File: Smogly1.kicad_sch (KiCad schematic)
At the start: 9 parts, among them J1 VCC IN, J10 NodeMCU A0-VIN, J11 NodeMCU D0-3.3V, J2 PMSx003, J3 BME280, J4 microUSB, J5 5/3.3/GND, J6 DeepSleep, J8 D5/6/7/8

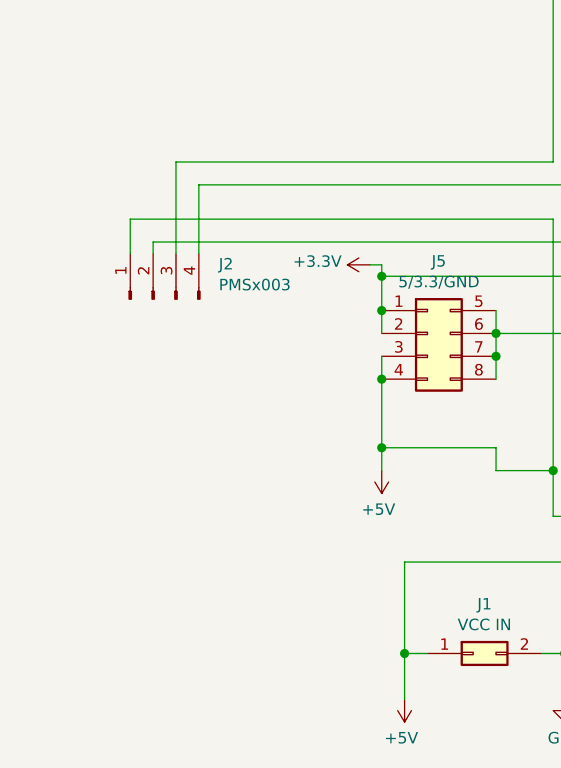
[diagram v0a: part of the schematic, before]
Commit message: added PMS7003 connector
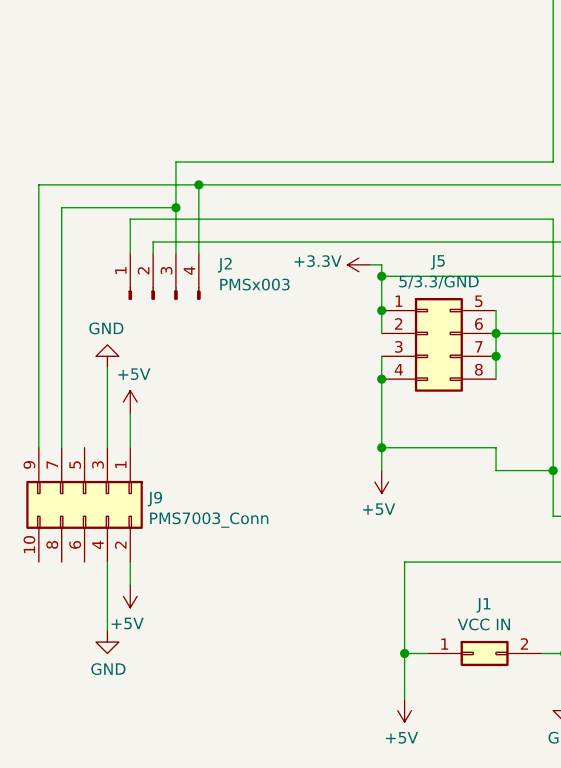
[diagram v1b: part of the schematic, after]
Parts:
- added J9: PMS7003_Conn, Connector_PinSocket_1.27mm:PinSocket_2x05_P1.27mm_Vertical, symbol Connector_Generic:Conn_02x05_Odd_Even
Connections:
- net +5V: now also J9.1 (Pin_1), J9.2 (Pin_2)
- net GND: now also J9.3 (Pin_3), J9.4 (Pin_4)
- net at J11.3 (Pin_3), J2.3 (Pin_3): now also J9.7 (Pin_7)
- net at J11.2 (Pin_2), J2.4 (Pin_4): now also J9.9 (Pin_9)
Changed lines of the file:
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@@
-(kicad_sch (version 20210126) (generator eeschema)
+(kicad_sch (version 20210406) (generator eeschema)
   (paper "A4")
+  (junction (at 88.9 123.19) (diameter 1.016) (color 0 0 0 0))
+  (junction (at 91.44 120.65) (diameter 1.016) (color 0 0 0 0))
   (junction (at 111.76 130.81) (diameter 1.016) (color 0 0 0 0))
   (junction (at 111.76 134.62) (diameter 1.016) (color 0 0 0 0))
@@
   (junction (at 132.08 172.72) (diameter 1.016) (color 0 0 0 0))
   (junction (at 133.35 137.16) (diameter 1.016) (color 0 0 0 0))
+  (wire (pts (xy 73.66 120.65) (xy 73.66 149.86))
+    (stroke (width 0) (type solid) (color 0 0 0 0))
+  )
+  (wire (pts (xy 76.2 123.19) (xy 76.2 149.86))
+    (stroke (width 0) (type solid) (color 0 0 0 0))
+  )
+  (wire (pts (xy 81.28 140.97) (xy 81.28 149.86))
+    (stroke (width 0) (type solid) (color 0 0 0 0))
+  )
+  (wire (pts (xy 81.28 162.56) (xy 81.28 170.18))
+    (stroke (width 0) (type solid) (color 0 0 0 0))
+  )
   (wire (pts (xy 83.82 124.46) (xy 83.82 128.27))
     (stroke (width 0) (type solid) (color 0 0 0 0))
   )
+  (wire (pts (xy 83.82 146.05) (xy 83.82 149.86))
+    (stroke (width 0) (type solid) (color 0 0 0 0))
+  )
+  (wire (pts (xy 83.82 162.56) (xy 83.82 165.1))
+    (stroke (width 0) (type solid) (color 0 0 0 0))
+  )
   (wire (pts (xy 86.36 127) (xy 86.36 128.27))
     (stroke (width 0) (type solid) (color 0 0 0 0))
   )
-  (wire (pts (xy 88.9 118.11) (xy 88.9 128.27))
+  (wire (pts (xy 88.9 118.11) (xy 88.9 123.19))
+    (stroke (width 0) (type solid) (color 0 0 0 0))
+  )
+  (wire (pts (xy 88.9 123.19) (xy 76.2 123.19))
+    (stroke (width 0) (type solid) (color 0 0 0 0))
+  )
+  (wire (pts (xy 88.9 123.19) (xy 88.9 128.27))
+    (stroke (width 0) (type solid) (color 0 0 0 0))
+  )
+  (wire (pts (xy 91.44 120.65) (xy 73.66 120.65))
     (stroke (width 0) (type solid) (color 0 0 0 0))
   )
@@
   (wire (pts (xy 250.19 113.03) (xy 254 113.03))
     (stroke (width 0) (type solid) (color 0 0 0 0))
+  )
+  (symbol (lib_id "power:+5V") (at 83.82 146.05 0) (unit 1)
+    (in_bom yes) (on_board yes)
+    (property "Reference" "#PWR0109" (id 0) (at 83.82 149.86 0)
+      (effects (font (size 1.27 1.27)) hide)
+    )
+    (property "Value" "+5V" (id 1) (at 84.1883 141.7256 0))
+    (property "Footprint" "" (id 2) (at 83.82 146.05 0)
+      (effects (font (size 1.27 1.27)) hide)
+    )
+    (property "Datasheet" "" (id 3) (at 83.82 146.05 0)
+      (effects (font (size 1.27 1.27)) hide)
+    )
+    (pin "1")
+  )
+  (symbol (lib_id "power:+5V") (at 83.82 165.1 180) (unit 1)
+    (in_bom yes) (on_board yes)
+    (property "Reference" "#PWR0106" (id 0) (at 83.82 161.29 0)
+      (effects (font (size 1.27 1.27)) hide)
+    )
+    (property "Value" "+5V" (id 1) (at 83.4517 169.4244 0))
+    (property "Footprint" "" (id 2) (at 83.82 165.1 0)
+      (effects (font (size 1.27 1.27)) hide)
+    )
+    (property "Datasheet" "" (id 3) (at 83.82 165.1 0)
+      (effects (font (size 1.27 1.27)) hide)
+    )
+    (pin "1")
   )
   (symbol (lib_id "power:+3.3V") (at 110.49 129.54 90) (unit 1)
@@
     )
     (property "Datasheet" "" (id 3) (at 114.3 177.8 0)
+      (effects (font (size 1.27 1.27)) hide)
+    )
+    (pin "1")
+  )
+  (symbol (lib_id "power:GND") (at 81.28 140.97 180) (unit 1)
+    (in_bom yes) (on_board yes)
+    (property "Reference" "#PWR0108" (id 0) (at 81.28 134.62 0)
+      (effects (font (size 1.27 1.27)) hide)
+    )
+    (property "Value" "GND" (id 1) (at 81.1657 136.6456 0))
+    (property "Footprint" "" (id 2) (at 81.28 140.97 0)
+      (effects (font (size 1.27 1.27)) hide)
+    )
+    (property "Datasheet" "" (id 3) (at 81.28 140.97 0)
+      (effects (font (size 1.27 1.27)) hide)
+    )
+    (pin "1")
+  )
+  (symbol (lib_id "power:GND") (at 81.28 170.18 0) (unit 1)
+    (in_bom yes) (on_board yes)
+    (property "Reference" "#PWR0107" (id 0) (at 81.28 176.53 0)
+      (effects (font (size 1.27 1.27)) hide)
+    )
+    (property "Value" "GND" (id 1) (at 81.3943 174.5044 0))
+    (property "Footprint" "" (id 2) (at 81.28 170.18 0)
+      (effects (font (size 1.27 1.27)) hide)
+    )
+    (property "Datasheet" "" (id 3) (at 81.28 170.18 0)
       (effects (font (size 1.27 1.27)) hide)
     )
@@
     (pin "7")
     (pin "8")
+  )
+  (symbol (lib_id "Connector_Generic:Conn_02x05_Odd_Even") (at 78.74 154.94 270) (unit 1)
+    (in_bom yes) (on_board yes) (fields_autoplaced)
+    (property "Reference" "J9" (id 0) (at 85.8521 155.4491 90)
+      (effects (font (size 1.27 1.27)) (justify left))
+    )
+    (property "Value" "PMS7003_Conn" (id 1) (at 85.8521 157.7478 90)
+      (effects (font (size 1.27 1.27)) (justify left))
+    )
+    (property "Footprint" "Connector_PinSocket_1.27mm:PinSocket_2x05_P1.27mm_Vertical" (id 2) (at 78.74 154.94 0)
+      (effects (font (size 1.27 1.27)) hide)
+    )
+    (property "Datasheet" "~" (id 3) (at 78.74 154.94 0)
+      (effects (font (size 1.27 1.27)) hide)
+    )
+    (pin "1")
+    (pin "10")
+    (pin "2")
+    (pin "3")
+    (pin "4")
+    (pin "5")
+    (pin "6")
+    (pin "7")
+    (pin "8")
+    (pin "9")
   )
   (symbol (lib_id "Connector:Conn_01x15_Female") (at 186.69 133.35 0) (unit 1)
@@
       (reference "#PWR0105") (unit 1) (value "GND") (footprint "")
     )
+    (path "/6c1cec05-3f16-472b-95f7-2e78858bbc8d"
+      (reference "#PWR0106") (unit 1) (value "+5V") (footprint "")
+    )
+    (path "/aec0c64b-ca04-492b-983b-4f91408467f6"
+      (reference "#PWR0107") (unit 1) (value "GND") (footprint "")
+    )
+    (path "/21ead478-6b8e-4711-b0c2-f5e2f2bf621d"
+      (reference "#PWR0108") (unit 1) (value "GND") (footprint "")
+    )
+    (path "/853f3b5d-9e5e-465a-b96e-9f74f0f409f2"
+      (reference "#PWR0109") (unit 1) (value "+5V") (footprint "")
+    )
     (path "/2aa0f8d3-f839-490b-9cac-1352fc599c36"
       (reference "J1") (unit 1) (value "VCC IN") (footprint "Connector_PinHeader_2.54mm:PinHeader_1x02_P2.54mm_Vertical")
@@
       (reference "J8") (unit 1) (value "D5/6/7/8") (footprint "Connector_PinHeader_2.54mm:PinHeader_1x04_P2.54mm_Vertical")
     )
+    (path "/66fa64c9-3338-4d0c-b796-5a118c8df9bb"
+      (reference "J9") (unit 1) (value "PMS7003_Conn") (footprint "Connector_PinSocket_1.27mm:PinSocket_2x05_P1.27mm_Vertical")
+    )
     (path "/6f75d4ab-abb1-468d-a83c-331e66e39c82"

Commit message: 12.05.2021
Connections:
- net +5V: now also J4.1 (Pin_1); no longer J4.5 (Pin_5)
- net GND: now also J4.5 (Pin_5); no longer J4.1 (Pin_1)
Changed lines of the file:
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@@
+    (stroke (width 0) (type solid) (color 0 0 0 0))
+  )
+  (wire (pts (xy 114.3 162.56) (xy 151.13 162.56))
     (stroke (width 0) (type solid) (color 0 0 0 0))
   )
@@
     (stroke (width 0) (type solid) (color 0 0 0 0))
   )
+  (wire (pts (xy 132.08 167.64) (xy 140.97 167.64))
+    (stroke (width 0) (type solid) (color 0 0 0 0))
+  )
   (wire (pts (xy 132.08 172.72) (xy 129.54 172.72))
     (stroke (width 0) (type solid) (color 0 0 0 0))
@@
     (stroke (width 0) (type solid) (color 0 0 0 0))
   )
-  (wire (pts (xy 140.97 162.56) (xy 114.3 162.56))
-    (stroke (width 0) (type solid) (color 0 0 0 0))
-  )
-  (wire (pts (xy 140.97 171.45) (xy 140.97 162.56))
+  (wire (pts (xy 140.97 167.64) (xy 140.97 171.45))
     (stroke (width 0) (type solid) (color 0 0 0 0))
   )
@@
     (stroke (width 0) (type solid) (color 0 0 0 0))
   )
-  (wire (pts (xy 151.13 167.64) (xy 132.08 167.64))
+  (wire (pts (xy 151.13 162.56) (xy 151.13 171.45))
     (stroke (width 0) (type solid) (color 0 0 0 0))
   )
-  (wire (pts (xy 151.13 171.45) (xy 151.13 167.64))
-    (stroke (width 0) (type solid) (color 0 0 0 0))
-  )

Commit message: ESP32 init
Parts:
- removed J6: DeepSleep, Connector_PinHeader_2.54mm:PinHeader_1x02_P2.54mm_Vertical, symbol Connector:Conn_01x02_Female
- J10: value NodeMCU A0-VIN -> ESP32-DevKit VIN-EN
- J11: value NodeMCU D0-3.3V -> ESP32-DevKit 3V3-D23
- J8: value D5/6/7/8 -> D33/32/35/35
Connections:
- net +3V3: now also J11.15 (Pin_15), J3.3 (Pin_3); no longer J10.11 (Pin_11)
- net at J2.3 (Pin_3), J9.7 (Pin_7): now also J11.2 (Pin_2); no longer J11.3 (Pin_3)
- net at J2.4 (Pin_4), J9.9 (Pin_9): now also J11.1 (Pin_1); no longer J11.2 (Pin_2)
- net at J8.1 (Pin_1): now also J10.4 (Pin_4); no longer J11.11 (Pin_11)
- net at J8.2 (Pin_2): now also J10.5 (Pin_5); no longer J11.10 (Pin_10)
- net at J8.3 (Pin_3): now also J10.6 (Pin_6); no longer J11.9 (Pin_9)
- net at J8.4 (Pin_4): now also J10.7 (Pin_7); no longer J11.8 (Pin_8)
- net at J11.14 (Pin_14): now also J3.4 (Pin_4)
- net at J11.4 (Pin_4): no longer J3.1 (Pin_1)
- net at J11.5 (Pin_5): no longer J3.2 (Pin_2)
- net at J11.6 (Pin_6): now also J3.1 (Pin_1); no longer J3.4 (Pin_4)
- net at J11.7 (Pin_7): now also J3.2 (Pin_2); no longer J3.3 (Pin_3)

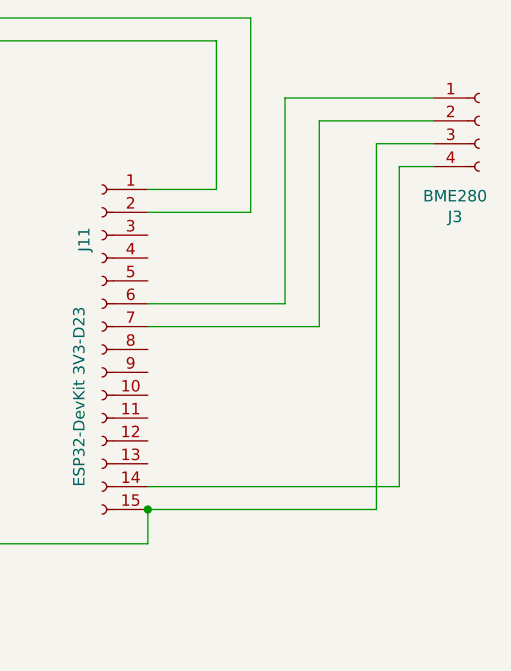
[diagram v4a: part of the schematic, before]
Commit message: fixed wrong BME280 power connection (switch +3/G pins)
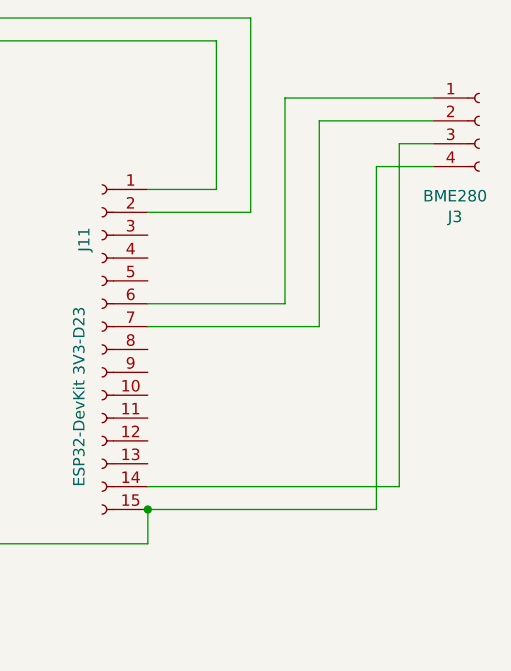
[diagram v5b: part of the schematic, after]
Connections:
- net +3V3: now also J3.4 (Pin_4); no longer J3.3 (Pin_3)
- net at J11.14 (Pin_14): now also J3.3 (Pin_3); no longer J3.4 (Pin_4)
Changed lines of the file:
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@@
     (stroke (width 0) (type solid) (color 0 0 0 0))
+  )
+  (wire (pts (xy 250.19 110.49) (xy 254 110.49))
+    (stroke (width 0) (type default) (color 0 0 0 0))
   )
   (wire (pts (xy 229.87 99.06) (xy 229.87 115.57))
@@
     (stroke (width 0) (type solid) (color 0 0 0 0))
   )
-  (wire (pts (xy 247.65 110.49) (xy 247.65 151.13))
-    (stroke (width 0) (type default) (color 0 0 0 0))
-  )
   (wire (pts (xy 171.45 151.13) (xy 171.45 157.48))
     (stroke (width 0) (type solid) (color 0 0 0 0))
@@
     (stroke (width 0) (type solid) (color 0 0 0 0))
   )
-  (wire (pts (xy 247.65 110.49) (xy 254 110.49))
-    (stroke (width 0) (type solid) (color 0 0 0 0))
-  )
   (wire (pts (xy 111.76 130.81) (xy 161.29 130.81))
     (stroke (width 0) (type solid) (color 0 0 0 0))
@@
     (stroke (width 0) (type solid) (color 0 0 0 0))
   )
-  (wire (pts (xy 250.19 113.03) (xy 254 113.03))
-    (stroke (width 0) (type solid) (color 0 0 0 0))
-  )
   (wire (pts (xy 91.44 128.27) (xy 91.44 120.65))
     (stroke (width 0) (type solid) (color 0 0 0 0))
@@
     (stroke (width 0) (type solid) (color 0 0 0 0))
   )
-  (wire (pts (xy 250.19 113.03) (xy 250.19 148.59))
-    (stroke (width 0) (type default) (color 0 0 0 0))
-  )
   (wire (pts (xy 111.76 142.24) (xy 111.76 149.86))
     (stroke (width 0) (type solid) (color 0 0 0 0))
@@
     (stroke (width 0) (type solid) (color 0 0 0 0))
   )
+  (wire (pts (xy 247.65 113.03) (xy 247.65 151.13))
+    (stroke (width 0) (type default) (color 0 0 0 0))
+  )
   (wire (pts (xy 111.76 149.86) (xy 111.76 152.4))
     (stroke (width 0) (type solid) (color 0 0 0 0))
@@
     (stroke (width 0) (type solid) (color 0 0 0 0))
   )
+  (wire (pts (xy 247.65 113.03) (xy 254 113.03))
+    (stroke (width 0) (type default) (color 0 0 0 0))
+  )
+  (wire (pts (xy 250.19 110.49) (xy 250.19 148.59))
+    (stroke (width 0) (type default) (color 0 0 0 0))
+  )
   (wire (pts (xy 130.81 118.11) (xy 88.9 118.11))
